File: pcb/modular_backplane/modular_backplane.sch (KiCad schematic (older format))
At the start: 63 parts, among them U1 DMP3028LK3-13, U2 DMP3028LK3-13, U4 NTD4969NT4G, U5 PREC024DAAN-RC, U6 mountingHole, U7 mountingHole, U8 mountingHole, U9 mountingHole

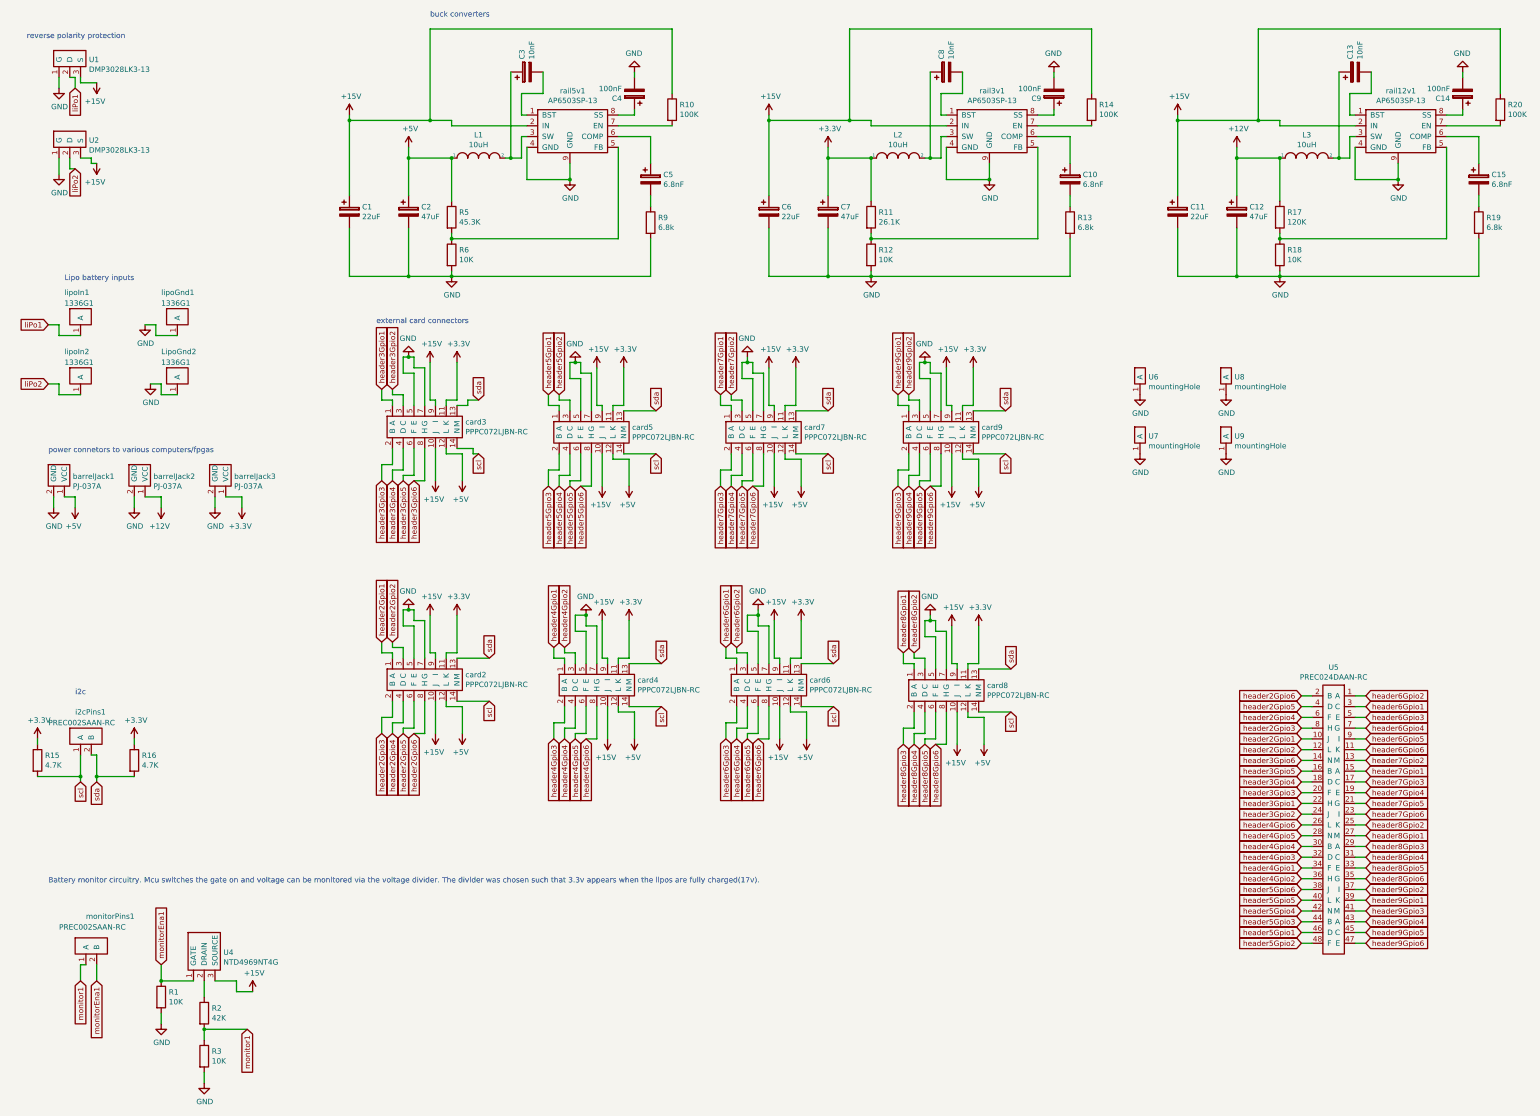
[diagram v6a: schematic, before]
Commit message: voltage divider
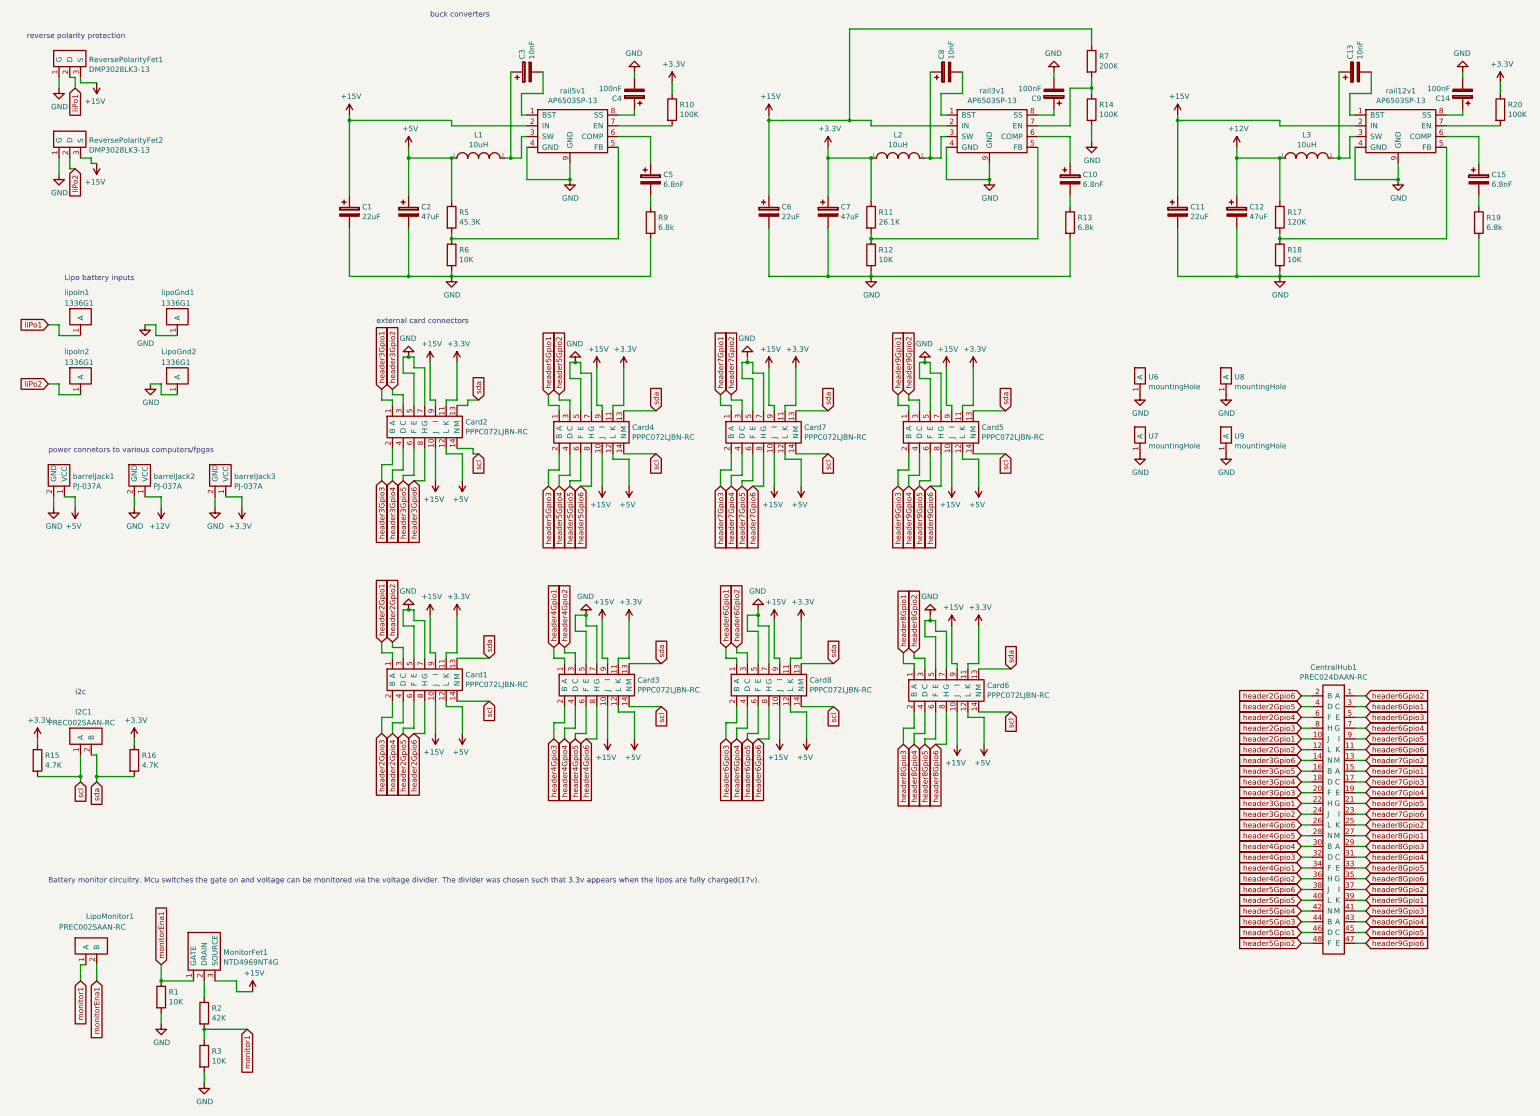
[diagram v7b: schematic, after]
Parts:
- added R7: 200K, Resistor_SMD:R_1206_3216Metric_Pad1.42x1.75mm_HandSolder, symbol Device:R
- renumbered card2 to Card1, card3 to Card2, card4 to Card3, card5 to Card4, card9 to Card5, card8 to Card6, card7 to Card7, card6 to Card8, U5 to CentralHub1, i2cPins1 to I2C1, monitorPins1 to LipoMonitor1, U4 to MonitorFet1, U1 to ReversePolarityFet1, U2 to ReversePolarityFet2
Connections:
- net +15V: now also R7.1; no longer R10.1, R14.1, R20.1
- net +3V3: now also R10.1, R20.1
- net GND: now also R14.2
- net at rail3v1.7 (EN): now also R14.1, R7.2; no longer R14.2
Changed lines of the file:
@@
 	1    0    0    -1
 $EndComp
-Wire Wire Line
-	6700 1750 6200 1750
 $Comp
 L power:+5V #PWR012
@@
 Wire Wire Line
 	6350 1650 6350 1600
-Wire Wire Line
-	6700 850  6700 1450
 $Comp
 L power:GND #PWR023
@@
 Wire Wire Line
 	4650 1750 4650 1700
-Wire Wire Line
-	4650 1700 4450 1700
 Connection ~ 3700 1700
 Wire Wire Line
@@
 Wire Wire Line
 	4650 1750 5350 1750
-Wire Wire Line
-	4450 850  4450 1700
-Wire Wire Line
-	4450 850  6700 850
-Connection ~ 4450 1700
-Wire Wire Line
-	4450 1700 3700 1700
 $Comp
 L backplane_Library:AP6503SP-13 rail3v1
@@
 	1    0    0    -1
 $EndComp
-Wire Wire Line
-	10600 1750 10100 1750
 $Comp
 L Device:R R12
@@
 Wire Wire Line
 	10250 1650 10250 1600
-Wire Wire Line
-	10600 850  10600 1450
 $Comp
 L power:GND #PWR039
@@
 Wire Wire Line
 	8550 1750 8550 1700
-Wire Wire Line
-	8550 1700 8350 1700
 Connection ~ 7600 1700
 Wire Wire Line
@@
 Wire Wire Line
 	8550 1750 9250 1750
-Wire Wire Line
-	8350 850  8350 1700
-Wire Wire Line
-	8350 850  10600 850
-Connection ~ 8350 1700
-Wire Wire Line
-	8350 1700 7600 1700
 $Comp
 L power:+3.3V #PWR030
@@
 $EndComp
 $Comp
-L backplane_Library:DMP3028LK3-13 U1
+L backplane_Library:DMP3028LK3-13 ReversePolarityFet1
 U 1 1 5C705B5E
 P 1150 1150
-F 0 "U1" H 1278 1165 50  0000 L CNN
+F 0 "ReversePolarityFet1" H 1278 1165 50  0000 L CNN
 F 1 "DMP3028LK3-13" H 1278 1074 50  0000 L CNN
 F 2 "backplane:DMP3028LK3-13" H 1150 1150 50  0001 C CNN
@@
 $EndComp
 $Comp
-L backplane_Library:DMP3028LK3-13 U2
+L backplane_Library:DMP3028LK3-13 ReversePolarityFet2
 U 1 1 5C705F48
 P 1150 1900
-F 0 "U2" H 1278 1915 50  0000 L CNN
+F 0 "ReversePolarityFet2" H 1278 1915 50  0000 L CNN
 F 1 "DMP3028LK3-13" H 1278 1824 50  0000 L CNN
 F 2 "backplane:DMP3028LK3-13" H 1150 1900 50  0001 C CNN
@@
 buck converters
 $Comp
-L backplane_Library:NTD4969NT4G U4
+L backplane_Library:NTD4969NT4G MonitorFet1
 U 1 1 5C8C8BB6
 P 2350 9700
-F 0 "U4" H 2528 9965 50  0000 L CNN
+F 0 "MonitorFet1" H 2528 9965 50  0000 L CNN
 F 1 "NTD4969NT4G" H 2528 9874 50  0000 L CNN
 F 2 "backplane:NTD4969NT4G" H 2350 9700 50  0001 C CNN
@@
 Battery monitor circuitry. Mcu switches the gate on and voltage can be monitored via the voltage divider. The divider was chosen such that 3.3v appears when the lipos are fully charged(17v).
 $Comp
-L backplane_Library:PREC002SAAN-RC monitorPins1
+L backplane_Library:PREC002SAAN-RC LipoMonitor1
 U 1 1 5C718C1D
 P 1300 9550
-F 0 "monitorPins1" H 1250 10000 50  0000 L CNN
+F 0 "LipoMonitor1" H 1250 10000 50  0000 L CNN
 F 1 "PREC002SAAN-RC" H 1000 9900 50  0000 L CNN
 F 2 "backplane:PREC002SAAN-RC" H 1300 9550 50  0001 C CNN
@@
 $EndComp
 $Comp
-L backplane_Library:PREC002SAAN-RC i2cPins1
+L backplane_Library:PREC002SAAN-RC I2C1
 U 1 1 5C4596BE
 P 1250 7600
-F 0 "i2cPins1" H 1150 8000 50  0000 L CNN
+F 0 "I2C1" H 1150 8000 50  0000 L CNN
 F 1 "PREC002SAAN-RC" H 900 7900 50  0000 L CNN
 F 2 "backplane:PREC002SAAN-RC" H 1250 7600 50  0001 C CNN
@@
 scl
 $Comp
-L backplane_Library:PPPC072LJBN-RC card3
+L backplane_Library:PPPC072LJBN-RC Card2
 U 1 1 5C63214A
 P 4350 4450
-F 0 "card3" H 4778 4396 50  0000 L CNN
+F 0 "Card2" H 4778 4396 50  0000 L CNN
 F 1 "PPPC072LJBN-RC" H 4778 4305 50  0000 L CNN
 F 2 "backplane:PPPC072LJBN-RC" H 4350 4700 50  0001 C CNN
@@
 scl
 $Comp
-L backplane_Library:PPPC072LJBN-RC card5
+L backplane_Library:PPPC072LJBN-RC Card4
 U 1 1 5C63FDF4
 P 5900 4500
-F 0 "card5" H 6328 4446 50  0000 L CNN
+F 0 "Card4" H 6328 4446 50  0000 L CNN
 F 1 "PPPC072LJBN-RC" H 6328 4355 50  0000 L CNN
 F 2 "backplane:PPPC072LJBN-RC" H 5900 4750 50  0001 C CNN
@@
 scl
 $Comp
-L backplane_Library:PPPC072LJBN-RC card7
+L backplane_Library:PPPC072LJBN-RC Card7
 U 1 1 5C651E2B
 P 7500 4500
-F 0 "card7" H 7928 4446 50  0000 L CNN
+F 0 "Card7" H 7928 4446 50  0000 L CNN
 F 1 "PPPC072LJBN-RC" H 7928 4355 50  0000 L CNN
 F 2 "backplane:PPPC072LJBN-RC" H 7500 4750 50  0001 C CNN
@@
 scl
 $Comp
-L backplane_Library:PPPC072LJBN-RC card9
+L backplane_Library:PPPC072LJBN-RC Card5
 U 1 1 5C66862C
 P 9150 4500
-F 0 "card9" H 9578 4446 50  0000 L CNN
+F 0 "Card5" H 9578 4446 50  0000 L CNN
 F 1 "PPPC072LJBN-RC" H 9578 4355 50  0000 L CNN
 F 2 "backplane:PPPC072LJBN-RC" H 9150 4750 50  0001 C CNN
@@
 scl
 $Comp
-L backplane_Library:PPPC072LJBN-RC card2
+L backplane_Library:PPPC072LJBN-RC Card1
 U 1 1 5C683A15
 P 4350 6800
-F 0 "card2" H 4778 6746 50  0000 L CNN
+F 0 "Card1" H 4778 6746 50  0000 L CNN
 F 1 "PPPC072LJBN-RC" H 4778 6655 50  0000 L CNN
 F 2 "backplane:PPPC072LJBN-RC" H 4350 7050 50  0001 C CNN
@@
 scl
 $Comp
-L backplane_Library:PPPC072LJBN-RC card4
+L backplane_Library:PPPC072LJBN-RC Card3
 U 1 1 5C6A7BEC
 P 5950 6850
-F 0 "card4" H 6378 6796 50  0000 L CNN
+F 0 "Card3" H 6378 6796 50  0000 L CNN
 F 1 "PPPC072LJBN-RC" H 6378 6705 50  0000 L CNN
 F 2 "backplane:PPPC072LJBN-RC" H 5950 7100 50  0001 C CNN
@@
 scl
 $Comp
-L backplane_Library:PPPC072LJBN-RC card6
+L backplane_Library:PPPC072LJBN-RC Card8
 U 1 1 5C6D4514
 P 7550 6850
-F 0 "card6" H 7978 6796 50  0000 L CNN
+F 0 "Card8" H 7978 6796 50  0000 L CNN
 F 1 "PPPC072LJBN-RC" H 7978 6705 50  0000 L CNN
 F 2 "backplane:PPPC072LJBN-RC" H 7550 7100 50  0001 C CNN
@@
 scl
 $Comp
-L backplane_Library:PPPC072LJBN-RC card8
+L backplane_Library:PPPC072LJBN-RC Card6
 U 1 1 5C709295
 P 9200 6900
-F 0 "card8" H 9628 6846 50  0000 L CNN
+F 0 "Card6" H 9628 6846 50  0000 L CNN
 F 1 "PPPC072LJBN-RC" H 9628 6755 50  0000 L CNN
 F 2 "backplane:PPPC072LJBN-RC" H 9200 7150 50  0001 C CNN
@@
 	1    0    0    -1
 $EndComp
-Wire Wire Line
-	14400 1750 13900 1750
 $Comp
 L Device:R R18
@@
 Wire Wire Line
 	14050 1650 14050 1600
-Wire Wire Line
-	14400 850  14400 1450
 $Comp
 L power:GND #PWR083
@@
 Wire Wire Line
 	12350 1750 12350 1700
-Wire Wire Line
-	12350 1700 12150 1700
 Connection ~ 11400 1700
 Wire Wire Line
@@
 Wire Wire Line
 	12350 1750 13050 1750
-Wire Wire Line
-	12150 850  12150 1700
-Wire Wire Line
-	12150 850  14400 850
-Connection ~ 12150 1700
-Wire Wire Line
-	12150 1700 11400 1700
 $Comp
 L power:+15V #PWR079
@@
 header6Gpio2
 $Comp
-L backplane_Library:PREC024DAAN-RC U5
+L backplane_Library:PREC024DAAN-RC CentralHub1
 U 1 1 5D038BC4
 P 12850 8150
-F 0 "U5" V 11485 8150 50  0000 C CNN
+F 0 "CentralHub1" V 11485 8150 50  0000 C CNN
 F 1 "PREC024DAAN-RC" V 11576 8150 50  0000 C CNN
 F 2 "backplane:PREC024DAAN-RC" H 12850 8350 50  0001 C CNN
@@
 	1    0    0    -1
 $EndComp
+Wire Wire Line
+	11400 1700 12350 1700
+Wire Wire Line
+	13900 1750 14400 1750
+Wire Wire Line
+	14400 1450 14400 1350
+Wire Wire Line
+	10100 1750 10400 1750
+Wire Wire Line
+	10400 1750 10400 1400
+$Comp
+L Device:R R7
+U 1 1 5C6814FA
+P 10600 1150
+F 0 "R7" H 10670 1196 50  0000 L CNN
+F 1 "200K" H 10670 1105 50  0000 L CNN
+F 2 "Resistor_SMD:R_1206_3216Metric_Pad1.42x1.75mm_HandSolder" V 10530 1150 50  0001 C CNN
+F 3 "~" H 10600 1150 50  0001 C CNN
+	1    10600 1150
+	1    0    0    -1
+$EndComp
+Wire Wire Line
+	10600 1900 10600 1750
+$Comp
+L power:GND #PWR020
+U 1 1 5C63D14F
+P 10600 1900
+F 0 "#PWR020" H 10600 1650 50  0001 C CNN
+F 1 "GND" H 10605 1727 50  0000 C CNN
+F 2 "" H 10600 1900 50  0001 C CNN
+F 3 "" H 10600 1900 50  0001 C CNN
+	1    10600 1900
+	1    0    0    -1
+$EndComp
+Wire Wire Line
+	10600 1400 10600 1450
+Wire Wire Line
+	10600 1300 10600 1400
+Connection ~ 10600 1400
+Wire Wire Line
+	10400 1400 10600 1400
+Wire Wire Line
+	8350 1700 7600 1700
+Wire Wire Line
+	8550 1700 8350 1700
+Connection ~ 8350 1700
+Wire Wire Line
+	8350 850  8350 1700
+Wire Wire Line
+	8350 850  10600 850
+Wire Wire Line
+	10600 1000 10600 850
+Wire Wire Line
+	3700 1700 4650 1700
+Wire Wire Line
+	6200 1750 6700 1750
+$Comp
+L power:+3.3V #PWR0105
+U 1 1 5C5F4E9C
+P 6700 1350
+F 0 "#PWR0105" H 6700 1200 50  0001 C CNN
+F 1 "+3.3V" H 6715 1523 50  0000 C CNN
+F 2 "" H 6700 1350 50  0001 C CNN
+F 3 "" H 6700 1350 50  0001 C CNN
+	1    6700 1350
+	1    0    0    -1
+$EndComp
+Wire Wire Line
+	6700 1450 6700 1350
+$Comp
+L power:+3.3V #PWR0106
+U 1 1 5C638002
+P 14400 1350
+F 0 "#PWR0106" H 14400 1200 50  0001 C CNN
+F 1 "+3.3V" H 14415 1523 50  0000 C CNN
+F 2 "" H 14400 1350 50  0001 C CNN
+F 3 "" H 14400 1350 50  0001 C CNN
+	1    14400 1350
+	1    0    0    -1
+$EndComp
